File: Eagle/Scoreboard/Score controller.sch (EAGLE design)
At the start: 21 parts, among them IC3 74HC595N, Q1 BD437, Q2 BD437, Q3 BD437, Q4 BD437, Q5 BD437, Q6 BD437, Q7 BD437

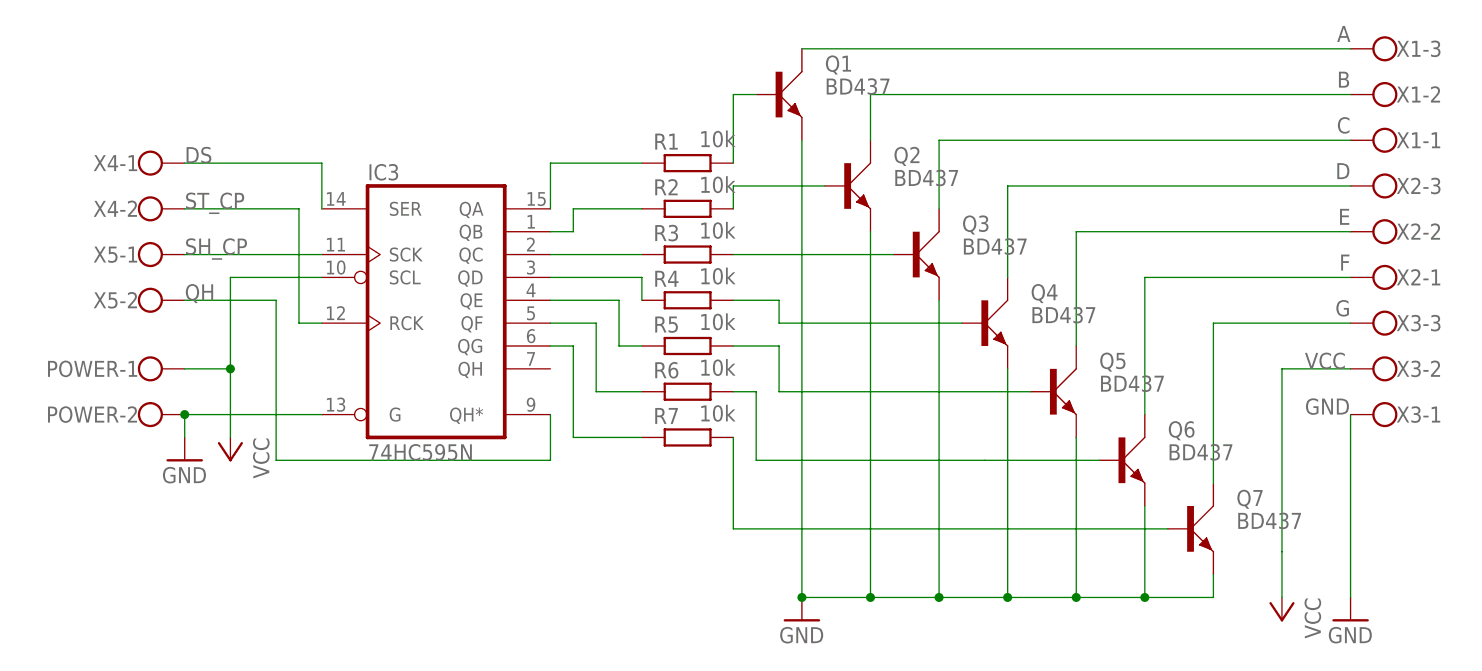
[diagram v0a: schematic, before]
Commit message: Changed transistor type for score controller, changed number of terminals to 8. Motherboard still TBD
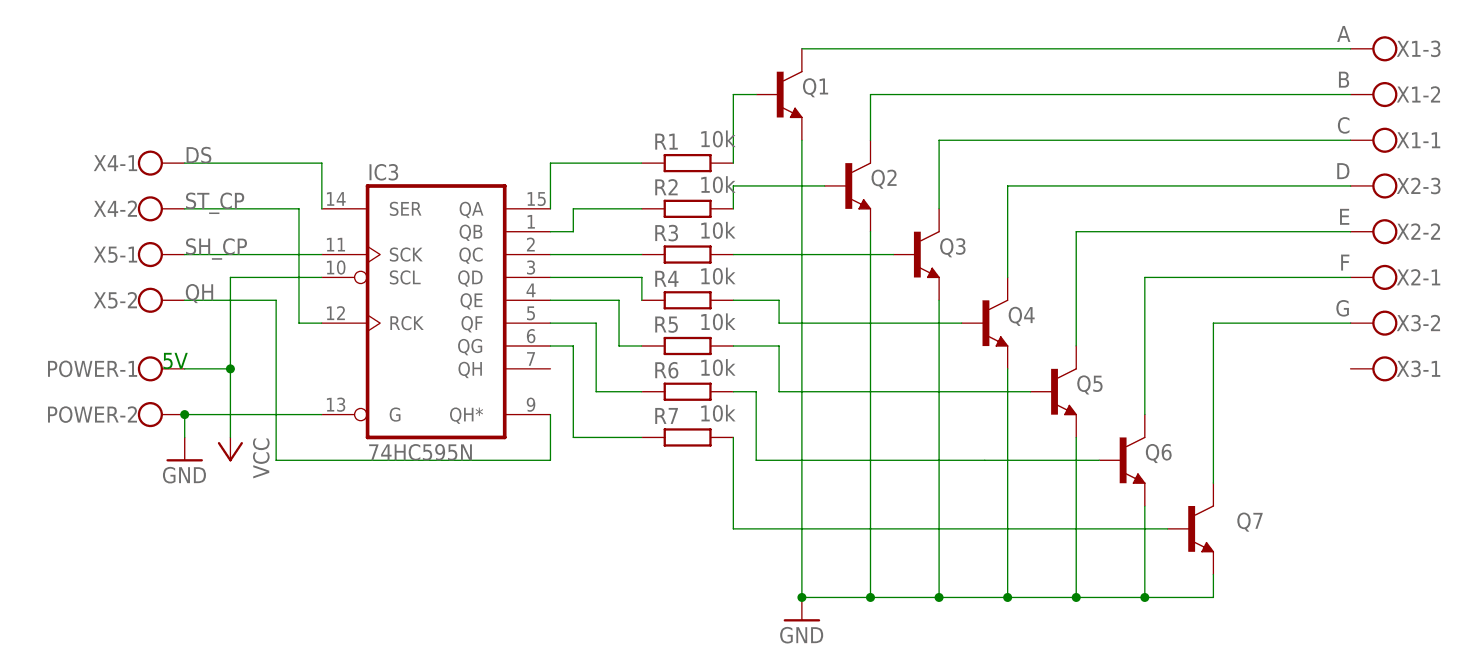
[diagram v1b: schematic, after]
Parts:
- Q1, Q2, Q3, Q4, Q5, Q6, Q7: value BD437 -> BD237TO126AV; device transistor-power:BD437 -> BD237:BD237TO126AV
- X3: device con-wago-500:W237-103 -> con-wago-500:W237-102
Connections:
- net G: now also X3-2.KL; no longer X3-3.KL
- net GND: no longer X3-1.KL
- net VCC: no longer X3-2.KL
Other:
- note added: "5V"
- moved on the sheet: X3-1, X3-2

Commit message: Chnaged all switch transistor to BC-337 TO92 AMMO
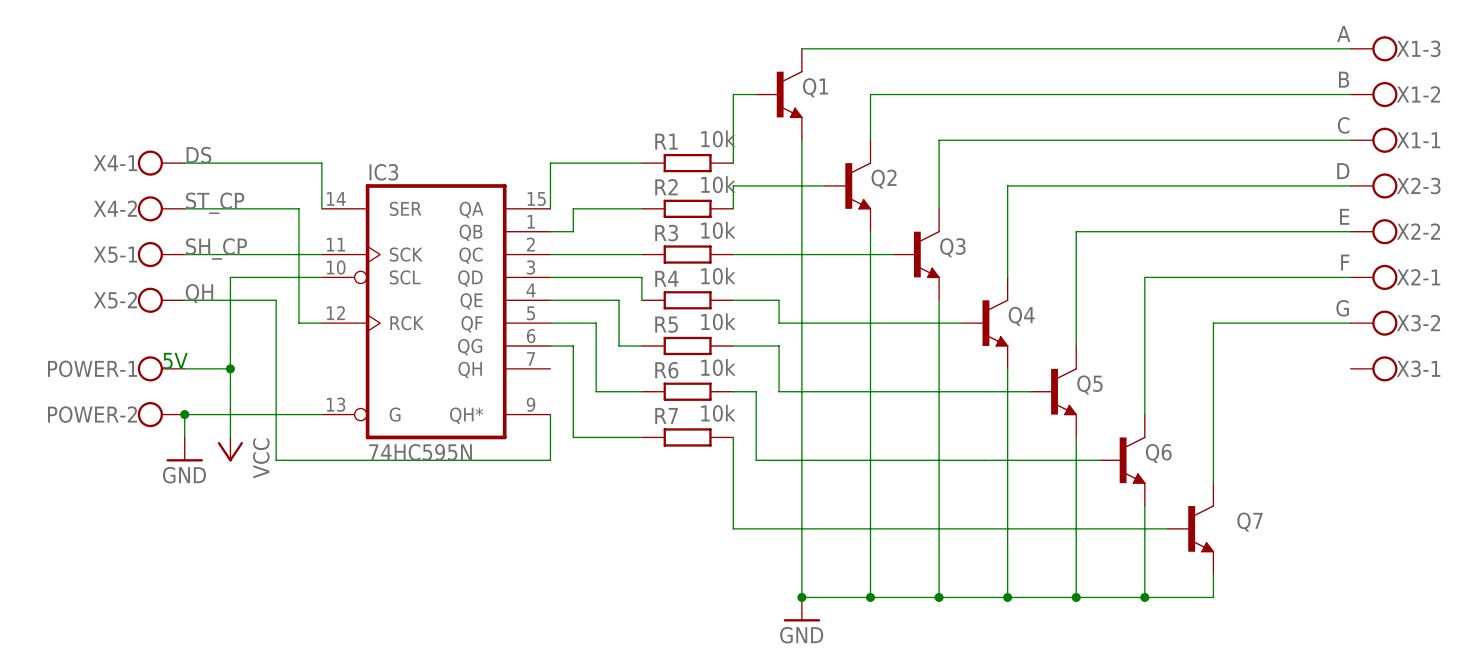
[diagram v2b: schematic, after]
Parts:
- Q1, Q2, Q3, Q4, Q5, Q6, Q7: value BD237TO126AV -> BC338-40; device BD237:BD237TO126AV -> transistor-npn:BC338-40
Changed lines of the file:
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@@
 <grid distance="0.1" unitdist="inch" unit="inch" style="lines" multiple="1" display="no" altdistance="0.01" altunitdist="inch" altunit="inch"/>
 <layers>
-<layer number="1" name="Top" color="4" fill="1" visible="no" active="no"/>
-<layer number="16" name="Bottom" color="1" fill="1" visible="no" active="no"/>
-<layer number="17" name="Pads" color="2" fill="1" visible="no" active="no"/>
-<layer number="18" name="Vias" color="2" fill="1" visible="no" active="no"/>
-<layer number="19" name="Unrouted" color="6" fill="1" visible="no" active="no"/>
-<layer number="20" name="Dimension" color="24" fill="1" visible="no" active="no"/>
-<layer number="21" name="tPlace" color="7" fill="1" visible="no" active="no"/>
-<layer number="22" name="bPlace" color="7" fill="1" visible="no" active="no"/>
-<layer number="23" name="tOrigins" color="15" fill="1" visible="no" active="no"/>
-<layer number="24" name="bOrigins" color="15" fill="1" visible="no" active="no"/>
-<layer number="25" name="tNames" color="7" fill="1" visible="no" active="no"/>
-<layer number="26" name="bNames" color="7" fill="1" visible="no" active="no"/>
-<layer number="27" name="tValues" color="7" fill="1" visible="no" active="no"/>
-<layer number="28" name="bValues" color="7" fill="1" visible="no" active="no"/>
+<layer number="1" name="Top" color="4" fill="1" visible="yes" active="no"/>
+<layer number="16" name="Bottom" color="1" fill="1" visible="yes" active="no"/>
+<layer number="17" name="Pads" color="2" fill="1" visible="yes" active="no"/>
+<layer number="18" name="Vias" color="2" fill="1" visible="yes" active="no"/>
+<layer number="19" name="Unrouted" color="6" fill="1" visible="yes" active="no"/>
+<layer number="20" name="Dimension" color="24" fill="1" visible="yes" active="no"/>
+<layer number="21" name="tPlace" color="7" fill="1" visible="yes" active="no"/>
+<layer number="22" name="bPlace" color="7" fill="1" visible="yes" active="no"/>
+<layer number="23" name="tOrigins" color="15" fill="1" visible="yes" active="no"/>
+<layer number="24" name="bOrigins" color="15" fill="1" visible="yes" active="no"/>
+<layer number="25" name="tNames" color="7" fill="1" visible="yes" active="no"/>
+<layer number="26" name="bNames" color="7" fill="1" visible="yes" active="no"/>
+<layer number="27" name="tValues" color="7" fill="1" visible="yes" active="no"/>
+<layer number="28" name="bValues" color="7" fill="1" visible="yes" active="no"/>
 <layer number="29" name="tStop" color="7" fill="3" visible="no" active="no"/>
 <layer number="30" name="bStop" color="7" fill="6" visible="no" active="no"/>
@@
 <layer number="35" name="tGlue" color="7" fill="4" visible="no" active="no"/>
 <layer number="36" name="bGlue" color="7" fill="5" visible="no" active="no"/>
-<layer number="37" name="tTest" color="7" fill="1" visible="no" active="no"/>
-<layer number="38" name="bTest" color="7" fill="1" visible="no" active="no"/>
+<layer number="37" name="tTest" color="7" fill="1" visible="yes" active="no"/>
+<layer number="38" name="bTest" color="7" fill="1" visible="yes" active="no"/>
 <layer number="39" name="tKeepout" color="4" fill="11" visible="no" active="no"/>
 <layer number="40" name="bKeepout" color="1" fill="11" visible="no" active="no"/>
@@
 <layer number="44" name="Drills" color="7" fill="1" visible="no" active="no"/>
 <layer number="45" name="Holes" color="7" fill="1" visible="no" active="no"/>
-<layer number="46" name="Milling" color="3" fill="1" visible="no" active="no"/>
-<layer number="47" name="Measures" color="7" fill="1" visible="no" active="no"/>
-<layer number="48" name="Document" color="7" fill="1" visible="no" active="no"/>
-<layer number="49" name="Reference" color="7" fill="1" visible="no" active="no"/>
-<layer number="51" name="tDocu" color="7" fill="1" visible="no" active="no"/>
-<layer number="52" name="bDocu" color="7" fill="1" visible="no" active="no"/>
+<layer number="46" name="Milling" color="3" fill="1" visible="yes" active="no"/>
+<layer number="47" name="Measures" color="7" fill="1" visible="yes" active="no"/>
+<layer number="48" name="Document" color="7" fill="1" visible="yes" active="no"/>
+<layer number="49" name="Reference" color="7" fill="1" visible="yes" active="no"/>
+<layer number="51" name="tDocu" color="7" fill="1" visible="yes" active="no"/>
+<layer number="52" name="bDocu" color="7" fill="1" visible="yes" active="no"/>
 <layer number="88" name="SimResults" color="9" fill="1" visible="yes" active="yes"/>
 <layer number="89" name="SimProbes" color="9" fill="1" visible="yes" active="yes"/>
@@
 <part name="R1" library="eagle-ltspice" library_urn="urn:adsk.eagle:library:217" deviceset="R" device="0204/7" package3d_urn="urn:adsk.eagle:package:13274/1" value="10k"/>
 <part name="POWER" library="con-wago-500" library_urn="urn:adsk.eagle:library:195" deviceset="W237-102" device="" package3d_urn="urn:adsk.eagle:package:10688/1"/>
-<part name="Q1" library="BD237" deviceset="BD237" device="TO126AV" value="BD237TO126AV"/>
+<part name="Q1" library="transistor-npn" library_urn="urn:adsk.eagle:library:398" deviceset="BC338*" device="" package3d_urn="urn:adsk.eagle:package:28989/2" technology="-40" value="BC338-40"/>
 <part name="IC3" library="74xx-eu" library_urn="urn:adsk.eagle:library:85" deviceset="74*595" device="N" package3d_urn="urn:adsk.eagle:package:2009/1" technology="HC"/>
 <part name="GND1" library="supply1" library_urn="urn:adsk.eagle:library:371" deviceset="GND" device=""/>
 <part name="P+1" library="supply1" library_urn="urn:adsk.eagle:library:371" deviceset="VCC" device=""/>
-<part name="Q2" library="BD237" deviceset="BD237" device="TO126AV" value="BD237TO126AV"/>
-<part name="Q3" library="BD237" deviceset="BD237" device="TO126AV" value="BD237TO126AV"/>
-<part name="Q4" library="BD237" deviceset="BD237" device="TO126AV" value="BD237TO126AV"/>
+<part name="Q2" library="transistor-npn" library_urn="urn:adsk.eagle:library:398" deviceset="BC338*" device="" package3d_urn="urn:adsk.eagle:package:28989/2" technology="-40" value="BC338-40"/>
+<part name="Q3" library="transistor-npn" library_urn="urn:adsk.eagle:library:398" deviceset="BC338*" device="" package3d_urn="urn:adsk.eagle:package:28989/2" technology="-40" value="BC338-40"/>
+<part name="Q4" library="transistor-npn" library_urn="urn:adsk.eagle:library:398" deviceset="BC338*" device="" package3d_urn="urn:adsk.eagle:package:28989/2" technology="-40" value="BC338-40"/>
 <part name="R2" library="eagle-ltspice" library_urn="urn:adsk.eagle:library:217" deviceset="R" device="0204/7" package3d_urn="urn:adsk.eagle:package:13274/1" value="10k"/>
 <part name="R3" library="eagle-ltspice" library_urn="urn:adsk.eagle:library:217" deviceset="R" device="0204/7" package3d_urn="urn:adsk.eagle:package:13274/1" value="10k"/>
@@
 <part name="R6" library="eagle-ltspice" library_urn="urn:adsk.eagle:library:217" deviceset="R" device="0204/7" package3d_urn="urn:adsk.eagle:package:13274/1" value="10k"/>
 <part name="R7" library="eagle-ltspice" library_urn="urn:adsk.eagle:library:217" deviceset="R" device="0204/7" package3d_urn="urn:adsk.eagle:package:13274/1" value="10k"/>
-<part name="Q5" library="BD237" deviceset="BD237" device="TO126AV" value="BD237TO126AV"/>
-<part name="Q6" library="BD237" deviceset="BD237" device="TO126AV" value="BD237TO126AV"/>
-<part name="Q7" library="BD237" deviceset="BD237" device="TO126AV" value="BD237TO126AV"/>
+<part name="Q5" library="transistor-npn" library_urn="urn:adsk.eagle:library:398" deviceset="BC338*" device="" package3d_urn="urn:adsk.eagle:package:28989/2" technology="-40" value="BC338-40"/>
+<part name="Q6" library="transistor-npn" library_urn="urn:adsk.eagle:library:398" deviceset="BC338*" device="" package3d_urn="urn:adsk.eagle:package:28989/2" technology="-40" value="BC338-40"/>
+<part name="Q7" library="transistor-npn" library_urn="urn:adsk.eagle:library:398" deviceset="BC338*" device="" package3d_urn="urn:adsk.eagle:package:28989/2" technology="-40" value="BC338-40"/>
 <part name="GND3" library="supply1" library_urn="urn:adsk.eagle:library:371" deviceset="GND" device=""/>
 <part name="X1" library="con-wago-500" library_urn="urn:adsk.eagle:library:195" deviceset="W237-103" device="" package3d_urn="urn:adsk.eagle:package:10691/1"/>
